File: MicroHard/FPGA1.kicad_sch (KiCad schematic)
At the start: 23 parts, among them U4 XC7A100T-FTG256, U5 MT25QL256ABA8ESF-0SIT, Y1 CB3-3C-20M000000

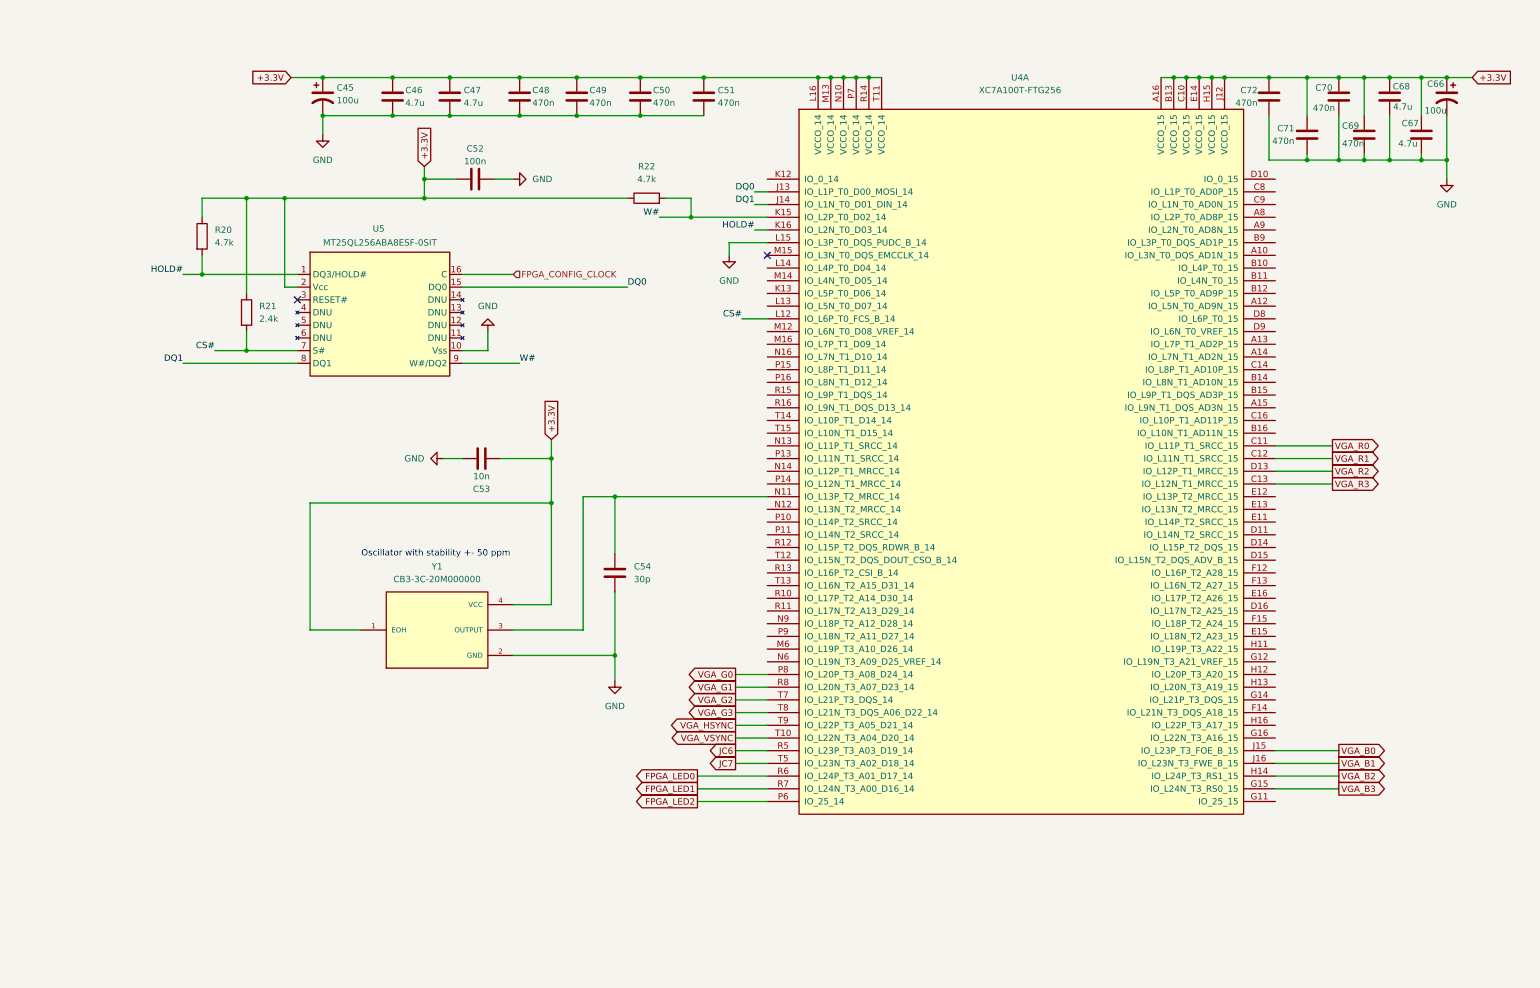
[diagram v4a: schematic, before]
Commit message: feat: VGA out lines from FPGA drawn
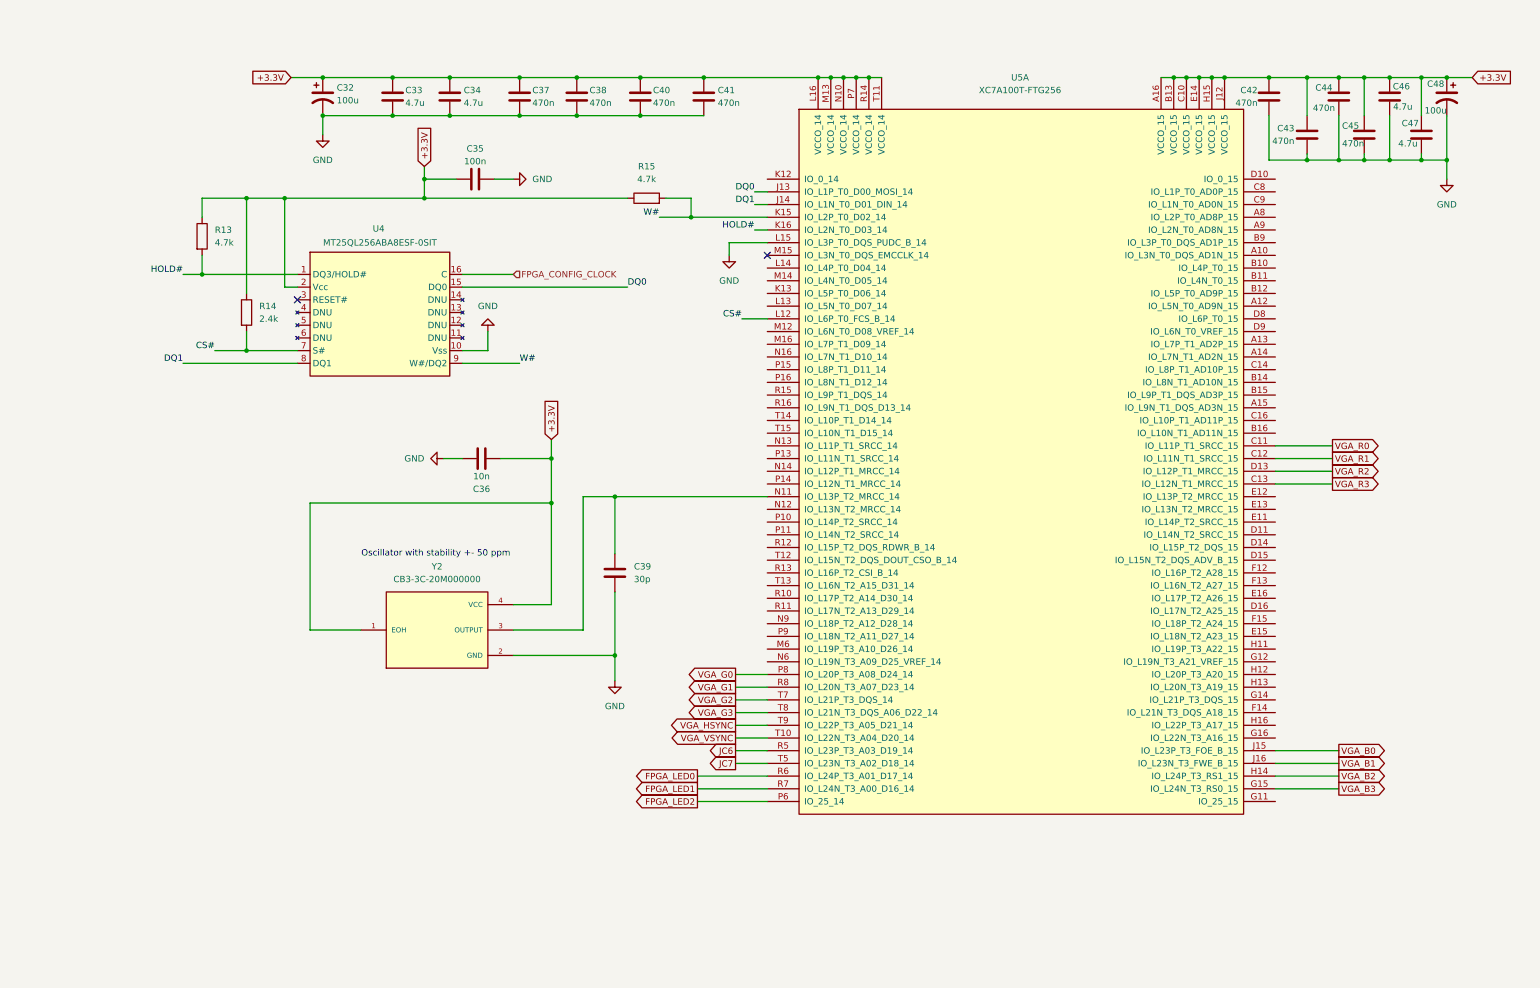
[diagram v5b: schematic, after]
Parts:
- renumbered C45 to C32, C46 to C33, C47 to C34, C52 to C35, C53 to C36, C48 to C37, C49 to C38, C54 to C39, C50 to C40, C51 to C41, C72 to C42, C71 to C43, C70 to C44, C69 to C45, C68 to C46, C67 to C47, C66 to C48, R20 to R13, R21 to R14, R22 to R15, U5 to U4, U4 to U5, Y1 to Y2

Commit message: feat: finished schematic, TODO: go through checklist
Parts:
- removed C39: 30p, symbol Device:C
- added C32, C35: 100n, symbol Device:C
- added IC1: IS66WVO32M8DBLL-166BLI, MicroHard:BGA24C100P5X5_600X800X120, symbol IS66WVO32M8DBLL-166BLI:IS66WVO32M8DBLL-166BLI
- added R13, R15: 2.4k, symbol Device:R
- U4: footprint (none) -> MicroHard:SOIC127P1032X265-16N
- U5: footprint (none) -> MicroHard:BGA256C100P16X16_1700X1700X155
- Y2: footprint CB3-3C-20M000000:OSC_CB3-3C-20M000000 -> MicroHard:OSC_CB3-3C-20M000000
- renumbered C32 to C33, C33 to C34, C34 to C37, C35 to C38, C37 to C40, C38 to C41, C40 to C42, C41 to C43, C42 to C44, C43 to C45, C44 to C46, C45 to C47, C46 to C48, C47 to C86, C48 to C87, R13 to R14, R14 to R66, R15 to R67
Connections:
- net +3.3V: now also C32.1, C35.1, IC1.B4 (VCC), IC1.D1 (VCCQ_1), IC1.E4 (VCCQ_2), R13.2, R15.2
- net FPGA_LED0: now also U5.H13 (IO_L20N_T3_A19_15); no longer U5.R6 (IO_L24P_T3_A01_D17_14)
- net FPGA_LED1: now also U5.G14 (IO_L21P_T3_DQS_15); no longer U5.R7 (IO_L24N_T3_A00_D16_14)
- net FPGA_LED2: now also U5.F14 (IO_L21N_T3_DQS_A18_15); no longer U5.P6 (IO_25_14)
- net GND: now also C32.2, C35.2, IC1.B3 (VSS), IC1.C1 (VSSQ_1), IC1.E5 (VSSQ_2)
- net SRAM_DQ4: now reaches U5.A14 (IO_L7N_T1_AD2N_15)
- net SRAM_DQ4: now also IC1.D5 (SIO4)
- net SRAM_DQ6: now reaches U5.B14 (IO_L8N_T1_AD10N_15)
- net SRAM_DQ6: now also IC1.E2 (SIO6)
- net SRAM_DQ7: now reaches U5.B15 (IO_L9P_T1_DQS_AD3P_15)
- net SRAM_DQ7: now also IC1.E1 (SIO7)
- net SRAM_DQ5: now reaches U5.C14 (IO_L8P_T1_AD10P_15)
- net SRAM_DQ5: now also IC1.E3 (SIO5)
- net SRAM_DQ0: now reaches U5.D16 (IO_L17N_T2_A25_15)
- net SRAM_DQ0: now also IC1.D3 (SIO0)
- net SRAM_SCLK: now reaches U5.E13 (IO_L13N_T2_MRCC_15)
- net SRAM_SCLK: now also IC1.B2 (SCLK)
- net SRAM_DQ2: now reaches U5.E15 (IO_L18N_T2_A23_15)
- net SRAM_DQ2: now also IC1.C4 (SIO2)
- net SRAM_DQSM: now reaches U5.E16 (IO_L17P_T2_A26_15)
- net SRAM_DQSM: now also IC1.C3 (DQSM)
- net SRAM_RESET#: now reaches U5.F12 (IO_L16P_T2_A28_15)
- net SRAM_RESET#: now also IC1.A4 (RESET#), R15.1
- net SRAM_CS#: now reaches U5.F13 (IO_L16N_T2_A27_15)
- net SRAM_CS#: now also IC1.A3 (CS#), R13.1
- net SRAM_DQ1: now reaches U5.F15 (IO_L18P_T2_A24_15)
- net SRAM_DQ1: now also IC1.D2 (SIO1)
- net SRAM_DQ3: now reaches U5.H11 (IO_L19P_T3_A22_15)
- net SRAM_DQ3: now also IC1.D4 (SIO3)
- net FPGA_US0_CLK: now reaches U5.N12 (IO_L13N_T2_MRCC_14)
- net FPGA_US0_TX: now reaches U5.R10 (IO_L17P_T2_A14_D30_14)
- net FPGA_US0_CS: now reaches U5.R11 (IO_L17N_T2_A13_D29_14)
- net FPGA_US0_RX: now reaches U5.T13 (IO_L16N_T2_A15_D31_14)
- net CS# renamed FLASH_CS#
- net DQ0 renamed FLASH_DQ0
- net DQ1 renamed FLASH_DQ1
- net HOLD# renamed FLASH_HOLD#
- net W# renamed FLASH_W#
- no-connect marks 2 -> 64
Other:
- note added: "Datasheet had one 0.01u for test circtuit but didnt specify anything more than that"
- note added: "Didnt specify capacitor"
- note added: "Flash Memory"
- note added: "Oscillator"
- note added: "PSRAM"
- note added: "Problem?"
- moved on the sheet: C36, Y2

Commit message: feat: completed schematic draft
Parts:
- removed C32, C35, C38: 100n, symbol Device:C
- removed IC1: IS66WVO32M8DBLL-166BLI, MicroHard:BGA24C100P5X5_600X800X120, symbol IS66WVO32M8DBLL-166BLI:IS66WVO32M8DBLL-166BLI
- removed R13, R15, R66: 2.4k, symbol Device:R
- removed R14, R67: 4.7k, symbol Device:R
- removed U4: MT25QL256ABA8ESF-0SIT, MicroHard:SOIC127P1032X265-16N, symbol MicroHardLibrary:MT25QL256ABA8ESF-0SIT
- added J?: FPGA_GPIO_header, Connector_JST:JST_XH_B8B-XH-AM_1x08_P2.50mm_Vertical, symbol Connector:Conn_01x08_Pin
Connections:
- net SRAM_CS#: now also U5.B11 (IO_L4N_T0_15); no longer U5.F13 (IO_L16N_T2_A27_15)
- net SRAM_DQ0: now also U5.A12 (IO_L5N_T0_AD9N_15); no longer U5.D16 (IO_L17N_T2_A25_15)
- net SRAM_DQ1: now also U5.D8 (IO_L6P_T0_15); no longer U5.F15 (IO_L18P_T2_A24_15)
- net SRAM_DQ2: now also U5.D9 (IO_L6N_T0_VREF_15); no longer U5.E15 (IO_L18N_T2_A23_15)
- net SRAM_DQ3: now also U5.A13 (IO_L7P_T1_AD2P_15); no longer U5.H11 (IO_L19P_T3_A22_15)
- net SRAM_DQSM: now also U5.B12 (IO_L5P_T0_AD9P_15); no longer U5.E16 (IO_L17P_T2_A26_15)
- net SRAM_RESET#: now also U5.B10 (IO_L4P_T0_15); no longer U5.F12 (IO_L16P_T2_A28_15)
- net at U5.D11 (IO_L14N_T2_SRCC_15): now also J?.3 (Pin_3)
- net at U5.D14 (IO_L15P_T2_DQS_15): now also J?.4 (Pin_4)
- net at U5.D15 (IO_L15N_T2_DQS_ADV_B_15): now also J?.5 (Pin_5)
- net at U5.E11 (IO_L14P_T2_SRCC_15): now also J?.2 (Pin_2)
- net at U5.E12 (IO_L13P_T2_MRCC_15): now also J?.1 (Pin_1)
- net FLASH_CS# renamed Flash Memory/FLASH_CS#
- net FLASH_DQ0 renamed Flash Memory/FLASH_DQ0
- net FLASH_DQ1 renamed Flash Memory/FLASH_DQ1
- net FLASH_HOLD# renamed Flash Memory/FLASH_HOLD#
- net FLASH_W# renamed Flash Memory/FLASH_W#
- new net: J?.8 (Pin_8), U5.E16 (IO_L17P_T2_A26_15)
- new net: J?.6 (Pin_6), U5.F12 (IO_L16P_T2_A28_15)
- new net: J?.7 (Pin_7), U5.F13 (IO_L16N_T2_A27_15)
- no-connect marks 64 -> 50
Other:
- added sheet Flash Memory (FlashMem.kicad_sch)
- added sheet SRAM (SRAM.kicad_sch)
- note added: "Does this mean both banks can be powered by same decoupling capacitors? One 47 μF (or 100 μF) capacitor is required for up to four V CCO banks when powered by the same voltage"
- note removed: "Datasheet had one 0.01u for test circtuit but didnt specify anything more than that"
- note removed: "Didnt specify capacitor"
- note removed: "Flash Memory"
- note removed: "Oscillator with stability +- 50 ppm"
- note removed: "PSRAM"
- note removed: "Problem?"
- moved on the sheet: C36, Y2

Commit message: Renumber parts
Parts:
- gave numbers to parts that had none: 1
- renumbered C33 to C32, C34 to C33, C36 to C34, C37 to C35, C40 to C36, C41 to C37, C42 to C38, C43 to C39, C44 to C40, C45 to C41, C46 to C42, C47 to C43, C48 to C44, C86 to C45, C87 to C46, U5 to U4
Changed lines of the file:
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@@
 		(on_board yes)
 		(dnp no)
-		(property "Reference" "C46"
+		(property "Reference" "C42"
 			(at 248.92 18.542 0)
 			(effects
@@
 			(project "MicroHard"
 				(path "/578bd531-a491-4b15-a479-460d159ffc14/e381883e-e672-4900-88a5-08b94f970a88/1131f32d-45e2-48d4-a5b0-b9e8f8db47f2"
-					(reference "C46")
+					(reference "C42")
 					(unit 1)
 				)
@@
 		(on_board yes)
 		(dnp no)
-		(property "Reference" "C43"
+		(property "Reference" "C39"
 			(at 125.984 19.05 0)
 			(effects
@@
 			(project "MicroHard"
 				(path "/578bd531-a491-4b15-a479-460d159ffc14/e381883e-e672-4900-88a5-08b94f970a88/1131f32d-45e2-48d4-a5b0-b9e8f8db47f2"
-					(reference "C43")
+					(reference "C39")
 					(unit 1)
 				)
@@
 		(on_board yes)
 		(dnp no)
-		(property "Reference" "C47"
+		(property "Reference" "C43"
 			(at 254.254 26.162 0)
 			(effects
@@
 			(project "MicroHard"
 				(path "/578bd531-a491-4b15-a479-460d159ffc14/e381883e-e672-4900-88a5-08b94f970a88/1131f32d-45e2-48d4-a5b0-b9e8f8db47f2"
-					(reference "C47")
+					(reference "C43")
 					(unit 1)
 				)
@@
 		(dnp no)
 		(fields_autoplaced yes)
-		(property "Reference" "#PWR025"
+		(property "Reference" "#PWR028"
 			(at 46.99 34.29 0)
 			(effects
@@
 			(project "MicroHard"
 				(path "/578bd531-a491-4b15-a479-460d159ffc14/e381883e-e672-4900-88a5-08b94f970a88/1131f32d-45e2-48d4-a5b0-b9e8f8db47f2"
-					(reference "#PWR025")
+					(reference "#PWR028")
 					(unit 1)
 				)
@@
 		(on_board yes)
 		(dnp no)
-		(property "Reference" "C86"
+		(property "Reference" "C45"
 			(at 266.192 25.654 0)
 			(effects
@@
 			(project "MicroHard"
 				(path "/578bd531-a491-4b15-a479-460d159ffc14/e381883e-e672-4900-88a5-08b94f970a88/1131f32d-45e2-48d4-a5b0-b9e8f8db47f2"
-					(reference "C86")
+					(reference "C45")
 					(unit 1)
 				)
@@
 		(dnp no)
 		(fields_autoplaced yes)
-		(property "Reference" "#PWR026"
+		(property "Reference" "#PWR029"
 			(at 49.53 83.82 0)
 			(effects
@@
 			(project "MicroHard"
 				(path "/578bd531-a491-4b15-a479-460d159ffc14/e381883e-e672-4900-88a5-08b94f970a88/1131f32d-45e2-48d4-a5b0-b9e8f8db47f2"
-					(reference "#PWR026")
+					(reference "#PWR029")
 					(unit 1)
 				)
@@
 		(on_board yes)
 		(dnp no)
-		(property "Reference" "C87"
+		(property "Reference" "C46"
 			(at 271.272 17.78 0)
 			(effects
@@
 			(project "MicroHard"
 				(path "/578bd531-a491-4b15-a479-460d159ffc14/e381883e-e672-4900-88a5-08b94f970a88/1131f32d-45e2-48d4-a5b0-b9e8f8db47f2"
-					(reference "C87")
+					(reference "C46")
 					(unit 1)
 				)
@@
 		(on_board yes)
 		(dnp no)
-		(property "Reference" "C36"
+		(property "Reference" "C34"
 			(at 60.452 85.09 90)
 			(effects
@@
 			(project "MicroHard"
 				(path "/578bd531-a491-4b15-a479-460d159ffc14/e381883e-e672-4900-88a5-08b94f970a88/1131f32d-45e2-48d4-a5b0-b9e8f8db47f2"
-					(reference "C36")
+					(reference "C34")
 					(unit 1)
 				)
@@
 		(on_board yes)
 		(dnp no)
-		(property "Reference" "C48"
+		(property "Reference" "C44"
 			(at 264.414 18.288 0)
 			(effects
@@
 			(project "MicroHard"
 				(path "/578bd531-a491-4b15-a479-460d159ffc14/e381883e-e672-4900-88a5-08b94f970a88/1131f32d-45e2-48d4-a5b0-b9e8f8db47f2"
-					(reference "C48")
+					(reference "C44")
 					(unit 1)
 				)
@@
 		(on_board yes)
 		(dnp no)
-		(property "Reference" "U5"
+		(property "Reference" "U4"
 			(at 186.436 16.51 0)
 			(effects
@@
 			(project "MicroHard"
 				(path "/578bd531-a491-4b15-a479-460d159ffc14/e381883e-e672-4900-88a5-08b94f970a88/1131f32d-45e2-48d4-a5b0-b9e8f8db47f2"
-					(reference "U5")
+					(reference "U4")
 					(unit 1)
 				)
@@
 		(on_board yes)
 		(dnp no)
-		(property "Reference" "C34"
+		(property "Reference" "C33"
 			(at 63.5 19.05 0)
 			(effects
@@
 			(project ""
 				(path "/578bd531-a491-4b15-a479-460d159ffc14/e381883e-e672-4900-88a5-08b94f970a88/1131f32d-45e2-48d4-a5b0-b9e8f8db47f2"
-					(reference "C34")
+					(reference "C33")
 					(unit 1)
 				)
@@
 		(dnp no)
 		(fields_autoplaced yes)
-		(property "Reference" "#PWR037"
+		(property "Reference" "#PWR031"
 			(at 128.27 58.42 0)
 			(effects
@@
 			(project ""
 				(path "/578bd531-a491-4b15-a479-460d159ffc14/e381883e-e672-4900-88a5-08b94f970a88/1131f32d-45e2-48d4-a5b0-b9e8f8db47f2"
-					(reference "#PWR037")
+					(reference "#PWR031")
 					(unit 1)
 				)
@@
 		(on_board yes)
 		(dnp no)
-		(property "Reference" "C45"
+		(property "Reference" "C41"
 			(at 241.3 26.67 0)
 			(effects
@@
 			(project "MicroHard"
 				(path "/578bd531-a491-4b15-a479-460d159ffc14/e381883e-e672-4900-88a5-08b94f970a88/1131f32d-45e2-48d4-a5b0-b9e8f8db47f2"
-					(reference "C45")
+					(reference "C41")
 					(unit 1)
 				)
@@
 		(on_board yes)
 		(dnp no)
-		(property "Reference" "C40"
+		(property "Reference" "C36"
 			(at 88.9 19.05 0)
 			(effects
@@
 			(project "MicroHard"
 				(path "/578bd531-a491-4b15-a479-460d159ffc14/e381883e-e672-4900-88a5-08b94f970a88/1131f32d-45e2-48d4-a5b0-b9e8f8db47f2"
-					(reference "C40")
+					(reference "C36")
 					(unit 1)
 				)
@@
 		(dnp no)
 		(fields_autoplaced yes)
-		(property "Reference" "#PWR061"
+		(property "Reference" "#PWR032"
 			(at 271.78 43.18 0)
 			(effects
@@
 			(project "MicroHard"
 				(path "/578bd531-a491-4b15-a479-460d159ffc14/e381883e-e672-4900-88a5-08b94f970a88/1131f32d-45e2-48d4-a5b0-b9e8f8db47f2"
-					(reference "#PWR061")
+					(reference "#PWR032")
 					(unit 1)
 				)
@@
 		(on_board yes)
 		(dnp no)
-		(property "Reference" "C37"
+		(property "Reference" "C35"
 			(at 75.184 19.05 0)
 			(effects
@@
 			(project "MicroHard"
 				(path "/578bd531-a491-4b15-a479-460d159ffc14/e381883e-e672-4900-88a5-08b94f970a88/1131f32d-45e2-48d4-a5b0-b9e8f8db47f2"
-					(reference "C37")
+					(reference "C35")
 					(unit 1)
 				)
@@
 		(on_board yes)
 		(dnp no)
-		(property "Reference" "C33"
+		(property "Reference" "C32"
 			(at 49.784 18.542 0)
 			(effects
@@
 			(project ""
 				(path "/578bd531-a491-4b15-a479-460d159ffc14/e381883e-e672-4900-88a5-08b94f970a88/1131f32d-45e2-48d4-a5b0-b9e8f8db47f2"
-					(reference "C33")
+					(reference "C32")
 					(unit 1)
 				)
@@
 		(on_board yes)
 		(dnp no)
-		(property "Reference" "J?"
+		(property "Reference" "J6"
 			(at 273.812 97.79 0)
 			(effects
@@
 			(project "MicroHard"
 				(path "/578bd531-a491-4b15-a479-460d159ffc14/e381883e-e672-4900-88a5-08b94f970a88/1131f32d-45e2-48d4-a5b0-b9e8f8db47f2"
-					(reference "J?")
+					(reference "J6")
 					(unit 1)
 				)
@@
 		(dnp no)
 		(fields_autoplaced yes)
-		(property "Reference" "#PWR027"
+		(property "Reference" "#PWR030"
 			(at 78.74 110.49 0)
 			(effects
@@
 			(project ""
 				(path "/578bd531-a491-4b15-a479-460d159ffc14/e381883e-e672-4900-88a5-08b94f970a88/1131f32d-45e2-48d4-a5b0-b9e8f8db47f2"
-					(reference "#PWR027")
+					(reference "#PWR030")
 					(unit 1)
 				)
@@
 		(on_board yes)
 		(dnp no)
-		(property "Reference" "C41"
+		(property "Reference" "C37"
 			(at 100.33 19.05 0)
 			(effects
@@
 			(project "MicroHard"
 				(path "/578bd531-a491-4b15-a479-460d159ffc14/e381883e-e672-4900-88a5-08b94f970a88/1131f32d-45e2-48d4-a5b0-b9e8f8db47f2"
-					(reference "C41")
+					(reference "C37")
 					(unit 1)
 				)
@@
 		(on_board yes)
 		(dnp no)
-		(property "Reference" "C44"
+		(property "Reference" "C40"
 			(at 233.934 19.05 0)
 			(effects
@@
 			(project "MicroHard"
 				(path "/578bd531-a491-4b15-a479-460d159ffc14/e381883e-e672-4900-88a5-08b94f970a88/1131f32d-45e2-48d4-a5b0-b9e8f8db47f2"
-					(reference "C44")
+					(reference "C40")
 					(unit 1)
 				)
@@
 		(on_board yes)
 		(dnp no)
-		(property "Reference" "C42"
+		(property "Reference" "C38"
 			(at 113.03 19.05 0)
 			(effects
@@
 			(project "MicroHard"
 				(path "/578bd531-a491-4b15-a479-460d159ffc14/e381883e-e672-4900-88a5-08b94f970a88/1131f32d-45e2-48d4-a5b0-b9e8f8db47f2"
-					(reference "C42")
-					(unit 1)
-				)
+					(reference "C38")
+					(unit 1)
+				)
